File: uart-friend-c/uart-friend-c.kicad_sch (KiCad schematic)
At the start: 22 parts, among them P1 USB_OTG, P3 CONN_01X03, P4 CONN_01X03, P5 CONN_01X06, P6 CONN_01X03, Q1 Q_PMOS_GSD, U1 AP7365_ADJ_SOT-23-5, U2 CY7C65213-SSOP

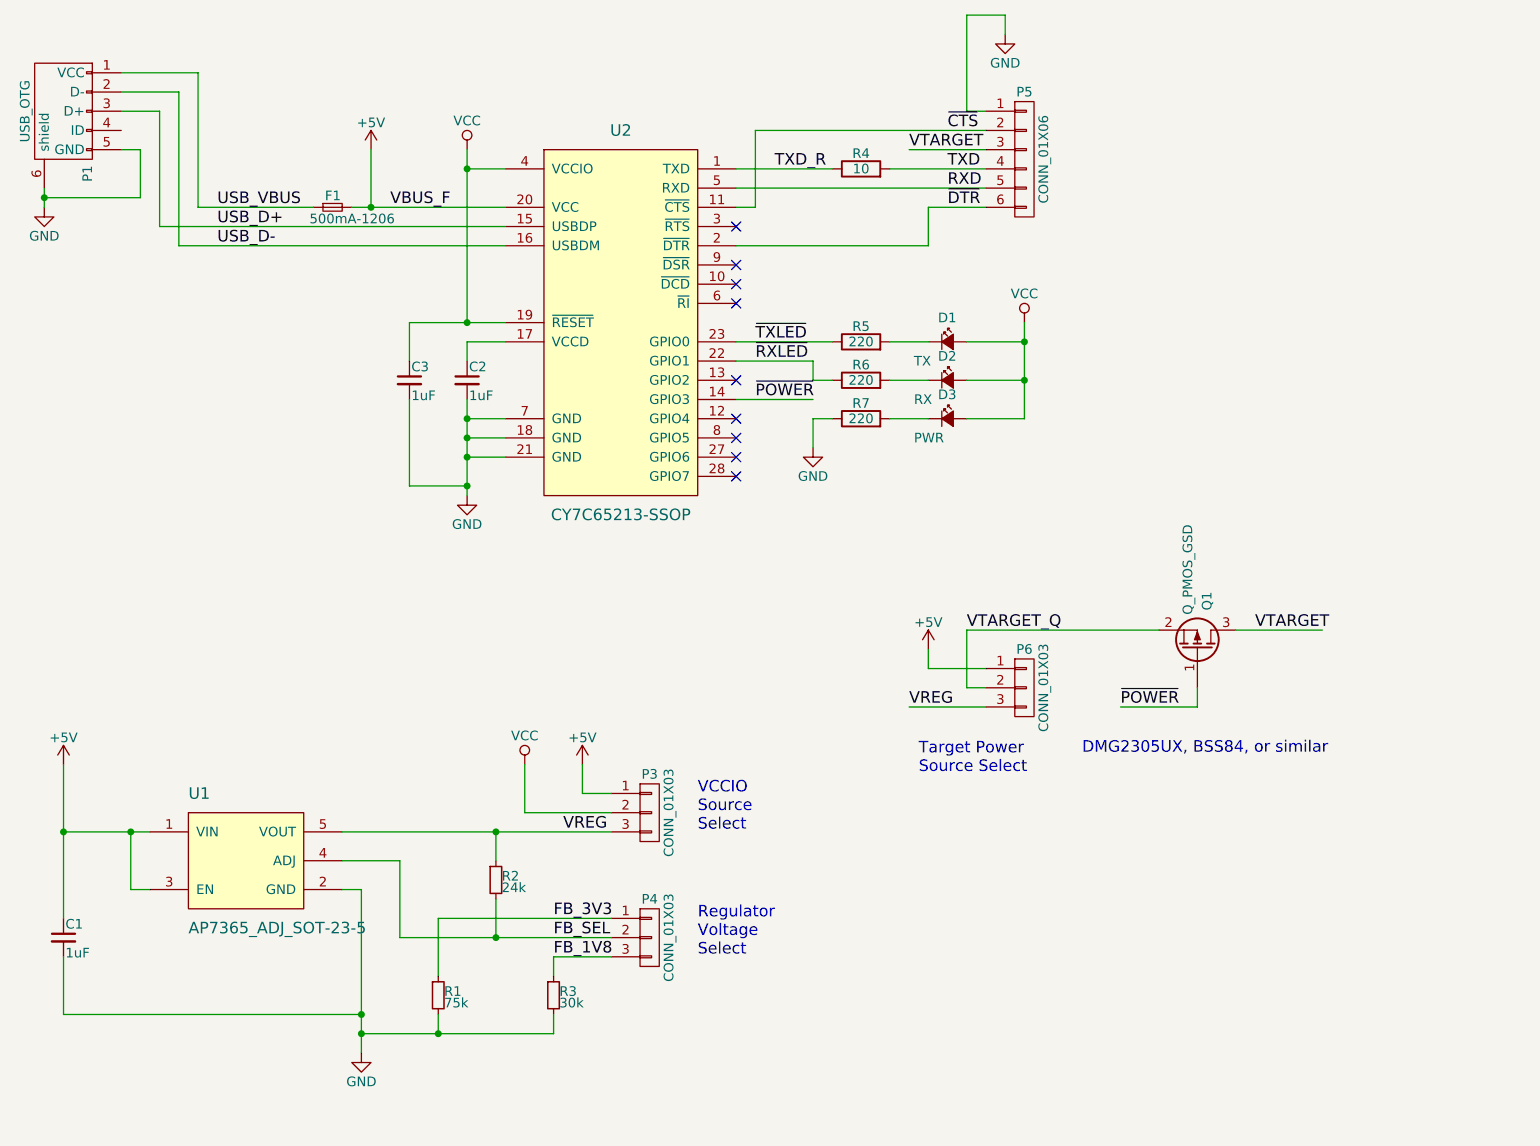
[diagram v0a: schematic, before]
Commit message: add uart-friend-c R1 design
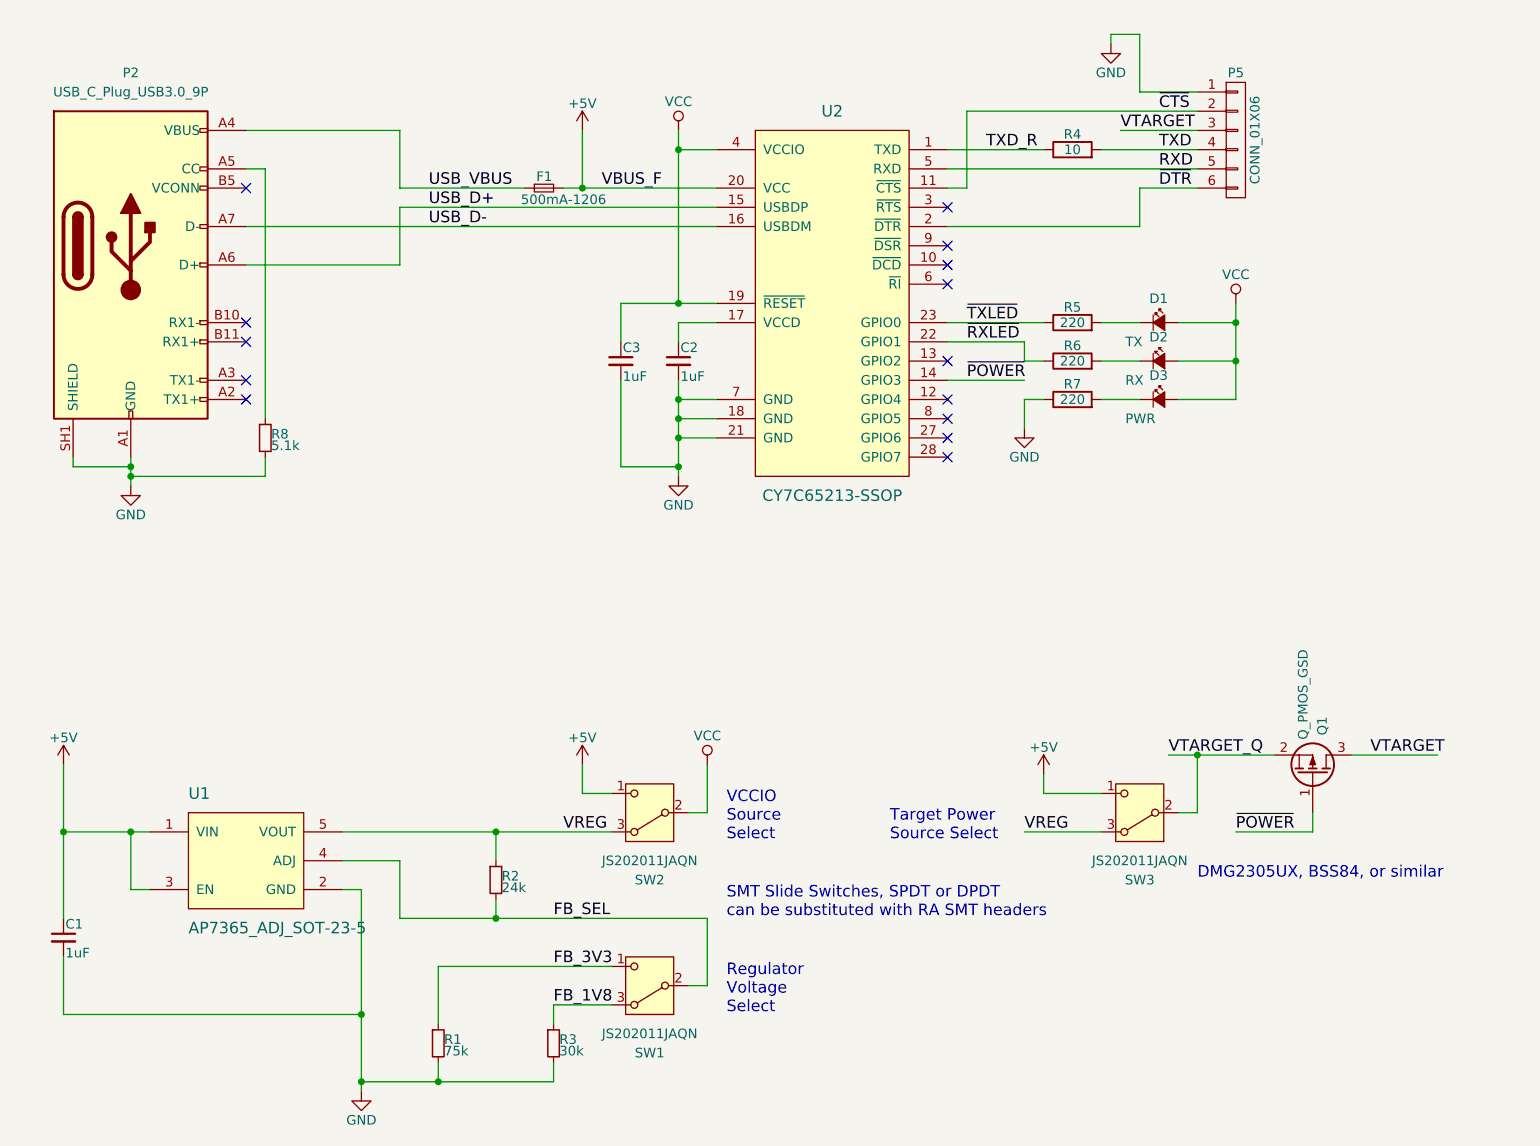
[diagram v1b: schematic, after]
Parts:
- removed P1: USB_OTG, Connect:USB_Micro-B, symbol uart-friend-rescue:USB_OTG
- removed P3, P4, P6: CONN_01X03, Pin_Headers:Pin_Header_Angled_1x03, symbol uart-friend-rescue:CONN_01X03
- added P2: USB_C_Plug_USB3.0_9P, uart-friend2-usb-special:USB_C_Plug_G-Switch_GT-USB-8016A_9P_TopMnt_Horizontal, symbol uart-friend2-usb:USB_C_Plug_USB3.0_9P
- added R8: 5.1k, Resistors_SMD:R_0805, symbol uart-friend-rescue:R_Small
- added SW1, SW2, SW3: JS202011JAQN, uart-friend-special:Switch_SPDT_P2.5mm_RA_SMD_8x9mm, symbol Switch:SW_SPDT_321
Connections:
- net +5V: now also SW2.1 (C), SW3.1 (C)
- net FB_1V8: now also SW1.3 (A)
- net FB_3V3: now also SW1.1 (C)
- net FB_SEL: now also SW1.2 (B)
- net GND: now also P2.A1 (GND), P2.A12 (GND), P2.B1 (GND), P2.B12 (GND), P2.SH1 (SHIELD), R8.2
- net USB_D+: now also P2.A6 (D+)
- net USB_D-: now also P2.A7 (D-)
- net USB_VBUS: now also P2.A4 (VBUS), P2.A9 (VBUS), P2.B4 (VBUS), P2.B9 (VBUS)
- net VCC: now also SW2.2 (B)
- net VREG: now also SW2.3 (A), SW3.3 (A)
- net VTARGET_Q: now also SW3.2 (B)
- new net: P2.A5 (CC), R8.1
- no-connect marks 9 -> 14
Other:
- note added: "SMT Slide Switches, SPDT or DPDT can be substituted with RA SMT headers"
- moved on the sheet: C2, C3, D1, D2, D3, F1, P5, Q1, R1, R3, R4, R5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
